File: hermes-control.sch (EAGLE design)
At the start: 77 parts, among them J1 1981568-1, J3 2201778-1, Q1 MMBT2222A, Q2 BC849SMD, Q3 FDN360P, Q4 FDN360P, Q5 BC849SMD, Q6 MMBT3906SOT23-3, Q7 FDN360P, Q8 MMBT2222A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

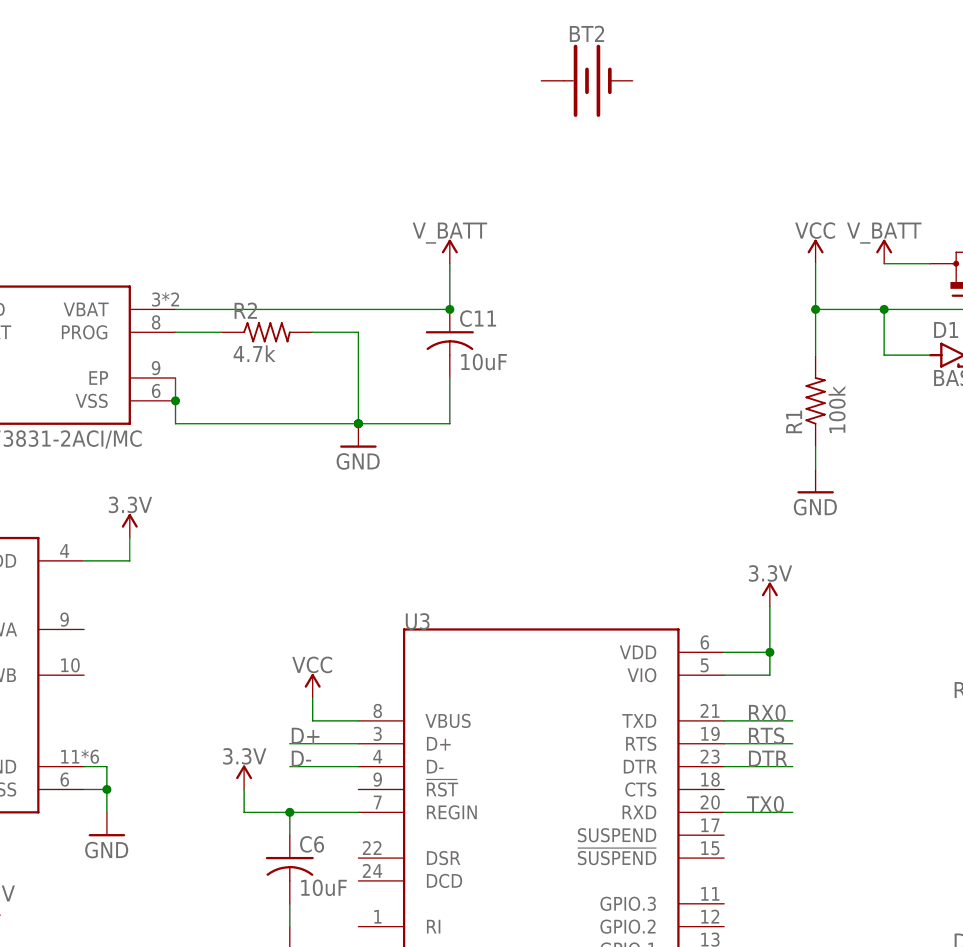
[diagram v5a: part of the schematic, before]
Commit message: routed single sides with no vias
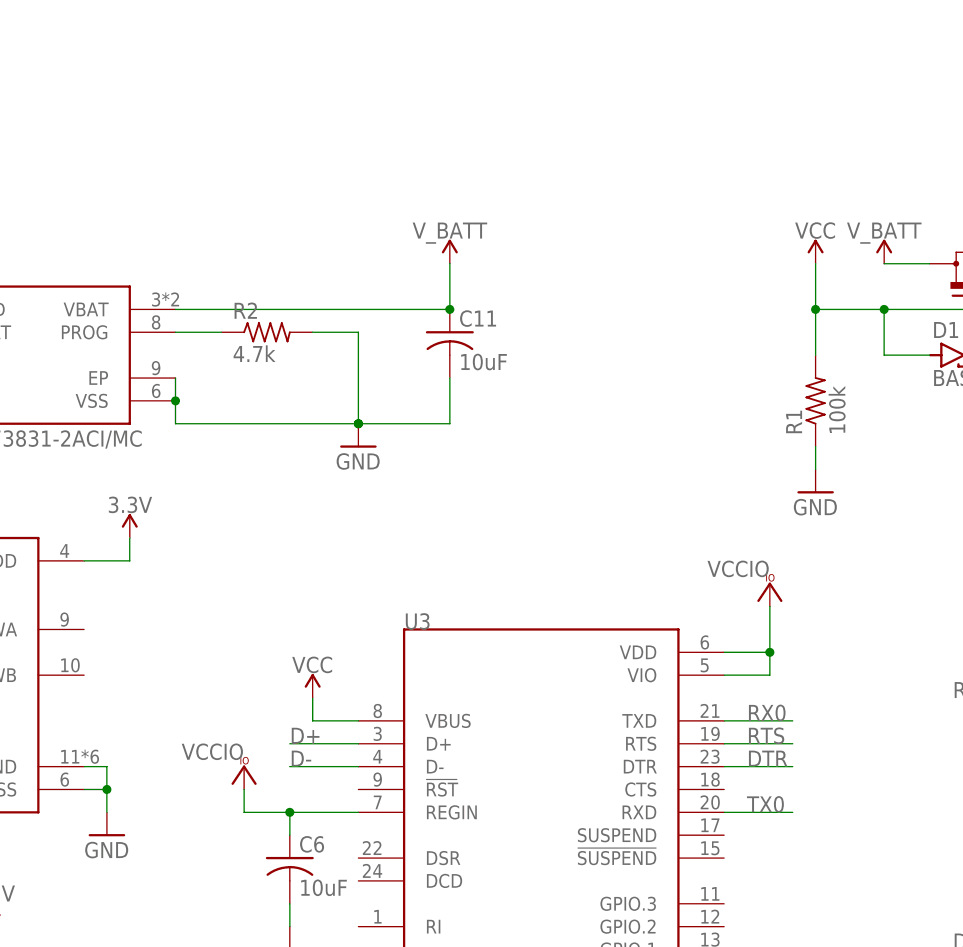
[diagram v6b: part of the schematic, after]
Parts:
- removed BT2: (no value), SparkFun-Batteries:BATTERY-18650
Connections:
- net 3.3V: no longer C6.1, U3.REGIN, U3.VDD, U3.VIO
- net VCCIO: now also C6.1, U3.REGIN, U3.VDD, U3.VIO
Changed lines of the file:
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@@
 <part name="R5" library="rcl" library_urn="urn:adsk.eagle:library:334" deviceset="R-US_" device="R0603" package3d_urn="urn:adsk.eagle:package:23555/3" value="4.7k"/>
 <part name="C6" library="rcl" library_urn="urn:adsk.eagle:library:334" deviceset="C-US" device="C0603" package3d_urn="urn:adsk.eagle:package:23616/2" value="10uF"/>
-<part name="SUPPLY10" library="SparkFun-PowerSymbols" library_urn="urn:adsk.eagle:library:530" deviceset="3.3V" device=""/>
 <part name="SUPPLY9" library="SparkFun-PowerSymbols" library_urn="urn:adsk.eagle:library:530" deviceset="VCC" device=""/>
 <part name="GND27" library="supply1" library_urn="urn:adsk.eagle:library:371" deviceset="GND" device=""/>
@@
 <part name="GND29" library="supply1" library_urn="urn:adsk.eagle:library:371" deviceset="GND" device=""/>
 <part name="SUPPLY27" library="SparkFun-PowerSymbols" library_urn="urn:adsk.eagle:library:530" deviceset="VCC" device=""/>
-<part name="SUPPLY28" library="SparkFun-PowerSymbols" library_urn="urn:adsk.eagle:library:530" deviceset="3.3V" device=""/>
 <part name="C9" library="rcl" library_urn="urn:adsk.eagle:library:334" deviceset="C-US" device="C0603" package3d_urn="urn:adsk.eagle:package:23616/2" value="10nF 16v"/>
 <part name="C15" library="rcl" library_urn="urn:adsk.eagle:library:334" deviceset="C-US" device="C0603" package3d_urn="urn:adsk.eagle:package:23616/2" value="100nF"/>
@@
 <part name="SUPPLY25" library="SparkFun-PowerSymbols" library_urn="urn:adsk.eagle:library:530" deviceset="3.3V" device=""/>
 <part name="SUPPLY29" library="SparkFun-PowerSymbols" library_urn="urn:adsk.eagle:library:530" deviceset="3.3V" device=""/>
-<part name="BT2" library="SparkFun-Batteries" library_urn="urn:adsk.eagle:library:508" deviceset="BATTERY" device="-18650" package3d_urn="urn:adsk.eagle:package:37227/1"/>
 <part name="S1" library="1437566-4" deviceset="1437566-4" device=""/>
 <part name="S2" library="1437566-4" deviceset="1437566-4" device=""/>
@@
 <part name="SUPPLY31" library="SparkFun-PowerSymbols" library_urn="urn:adsk.eagle:library:530" deviceset="3.3V" device=""/>
 <part name="GND11" library="supply1" library_urn="urn:adsk.eagle:library:371" deviceset="GND" device=""/>
+<part name="VCC4" library="supply1" library_urn="urn:adsk.eagle:library:371" deviceset="VCCIO" device=""/>
+<part name="VCC5" library="supply1" library_urn="urn:adsk.eagle:library:371" deviceset="VCCIO" device=""/>
 </parts>
 <sheets>
@@
 <attribute name="VALUE" x="148.336" y="102.489" size="1.778" layer="96"/>
 </instance>
-<instance part="SUPPLY10" gate="G$1" x="142.24" y="114.3" smashed="yes">
-<attribute name="VALUE" x="142.24" y="117.094" size="1.778" layer="96" align="bottom-center"/>
-</instance>
 <instance part="SUPPLY9" gate="G$1" x="149.86" y="124.46" smashed="yes">
 <attribute name="VALUE" x="149.86" y="127.254" size="1.778" layer="96" align="bottom-center"/>
@@
 <instance part="SUPPLY27" gate="G$1" x="86.36" y="86.36" smashed="yes">
 <attribute name="VALUE" x="86.36" y="89.154" size="1.778" layer="96" align="bottom-center"/>
-</instance>
-<instance part="SUPPLY28" gate="G$1" x="200.66" y="134.62" smashed="yes">
-<attribute name="VALUE" x="200.66" y="137.414" size="1.778" layer="96" align="bottom-center"/>
 </instance>
 <instance part="C9" gate="G$1" x="421.64" y="101.6" smashed="yes">
@@
 <attribute name="VALUE" x="43.18" y="106.934" size="1.778" layer="96" align="bottom-center"/>
 </instance>
-<instance part="BT2" gate="G$1" x="180.34" y="193.04" smashed="yes">
-<attribute name="NAME" x="180.34" y="197.358" size="1.778" layer="95" font="vector" align="bottom-center"/>
-<attribute name="VALUE" x="180.34" y="188.722" size="1.778" layer="96" font="vector" align="top-center"/>
-</instance>
 <instance part="S1" gate="G$1" x="358.14" y="170.18" smashed="yes">
 <attribute name="NAME" x="353.055809375" y="174.75576875" size="1.77946875" layer="95"/>
@@
 <instance part="GND11" gate="1" x="355.6" y="25.4" smashed="yes">
 <attribute name="VALUE" x="353.06" y="22.86" size="1.778" layer="96"/>
+</instance>
+<instance part="VCC4" gate="G$1" x="200.66" y="137.16" smashed="yes">
+<attribute name="VALUE" x="200.66" y="139.7" size="1.778" layer="96" rot="R180"/>
+</instance>
+<instance part="VCC5" gate="G$1" x="142.24" y="116.84" smashed="yes">
+<attribute name="VALUE" x="142.24" y="119.38" size="1.778" layer="96" rot="R180"/>
 </instance>
 </instances>
@@
 </segment>
 <segment>
-<pinref part="SUPPLY10" gate="G$1" pin="3.3V"/>
-<wire x1="142.24" y1="111.76" x2="142.24" y2="114.3" width="0.1524" layer="91"/>
-<pinref part="U3" gate="G$1" pin="REGIN"/>
-<wire x1="154.94" y1="111.76" x2="147.32" y2="111.76" width="0.1524" layer="91"/>
-<pinref part="C6" gate="G$1" pin="1"/>
-<wire x1="147.32" y1="111.76" x2="147.32" y2="109.22" width="0.1524" layer="91"/>
-<wire x1="147.32" y1="111.76" x2="142.24" y2="111.76" width="0.1524" layer="91"/>
-<junction x="147.32" y="111.76"/>
-</segment>
-<segment>
 <pinref part="R12" gate="G$1" pin="2"/>
 <pinref part="SUPPLY26" gate="G$1" pin="3.3V"/>
@@
 <wire x1="106.68" y1="96.52" x2="114.3" y2="96.52" width="0.1524" layer="91"/>
 <junction x="114.3" y="96.52"/>
-</segment>
-<segment>
-<pinref part="U3" gate="G$1" pin="VIO"/>
-<wire x1="195.58" y1="127" x2="200.66" y2="127" width="0.1524" layer="91"/>
-<wire x1="200.66" y1="127" x2="200.66" y2="129.54" width="0.1524" layer="91"/>
-<pinref part="U3" gate="G$1" pin="VDD"/>
-<wire x1="200.66" y1="129.54" x2="195.58" y2="129.54" width="0.1524" layer="91"/>
-<pinref part="SUPPLY28" gate="G$1" pin="3.3V"/>
-<wire x1="200.66" y1="134.62" x2="200.66" y2="129.54" width="0.1524" layer="91"/>
-<junction x="200.66" y="129.54"/>
 </segment>
 <segment>
@@
 <pinref part="VCC3" gate="G$1" pin="VCCIO"/>
 </segment>
-</net>
+<segment>
+<pinref part="U3" gate="G$1" pin="VIO"/>
+<wire x1="195.58" y1="127" x2="200.66" y2="127" width="0.1524" layer="91"/>
+<wire x1="200.66" y1="127" x2="200.66" y2="129.54" width="0.1524" layer="91"/>
+<pinref part="U3" gate="G$1" pin="VDD"/>
+<wire x1="200.66" y1="129.54" x2="195.58" y2="129.54" width="0.1524" layer="91"/>
+<wire x1="200.66" y1="134.62" x2="200.66" y2="129.54" width="0.1524" layer="91"/>
+<junction x="200.66" y="129.54"/>
+<pinref part="VCC4" gate="G$1" pin="VCCIO"/>
+</segment>
+<segment>
+<wire x1="142.24" y1="111.76" x2="142.24" y2="114.3" width="0.1524" layer="91"/>
+<pinref part="U3" gate="G$1" pin="REGIN"/>
+<wire x1="154.94" y1="111.76" x2="147.32" y2="111.76" width="0.1524" layer="91"/>
+<pinref part="C6" gate="G$1" pin="1"/>
+<wire x1="147.32" y1="111.76" x2="147.32" y2="109.22" width="0.1524" layer="91"/>
+<wire x1="147.32" y1="111.76" x2="142.24" y2="111.76" width="0.1524" layer="91"/>
+<junction x="147.32" y="111.76"/>
+<pinref part="VCC5" gate="G$1" pin="VCCIO"/>
+</segment>
+</net>
